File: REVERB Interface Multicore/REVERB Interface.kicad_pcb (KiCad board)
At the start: 2 copper layers, 90.2 x 95.9 mm, 69 parts, among them J1 RPiZeroW, J2 Iridium, J3 APRS, J4 Antenna, J5 UPDI, J6 USBPWR, M1 Stack Mounting Hole, M2 Stack Mounting Hole, M3 Stack Mounting Hole, M4 Stack Mounting Hole, M5 PiMount, M6 PiMount, M7 PiMount, M8 PiMount, U1 IMU, U2 MAX3232, U3 ATtiny1604-SS, U4 TXB0104D, U5 DS3232M

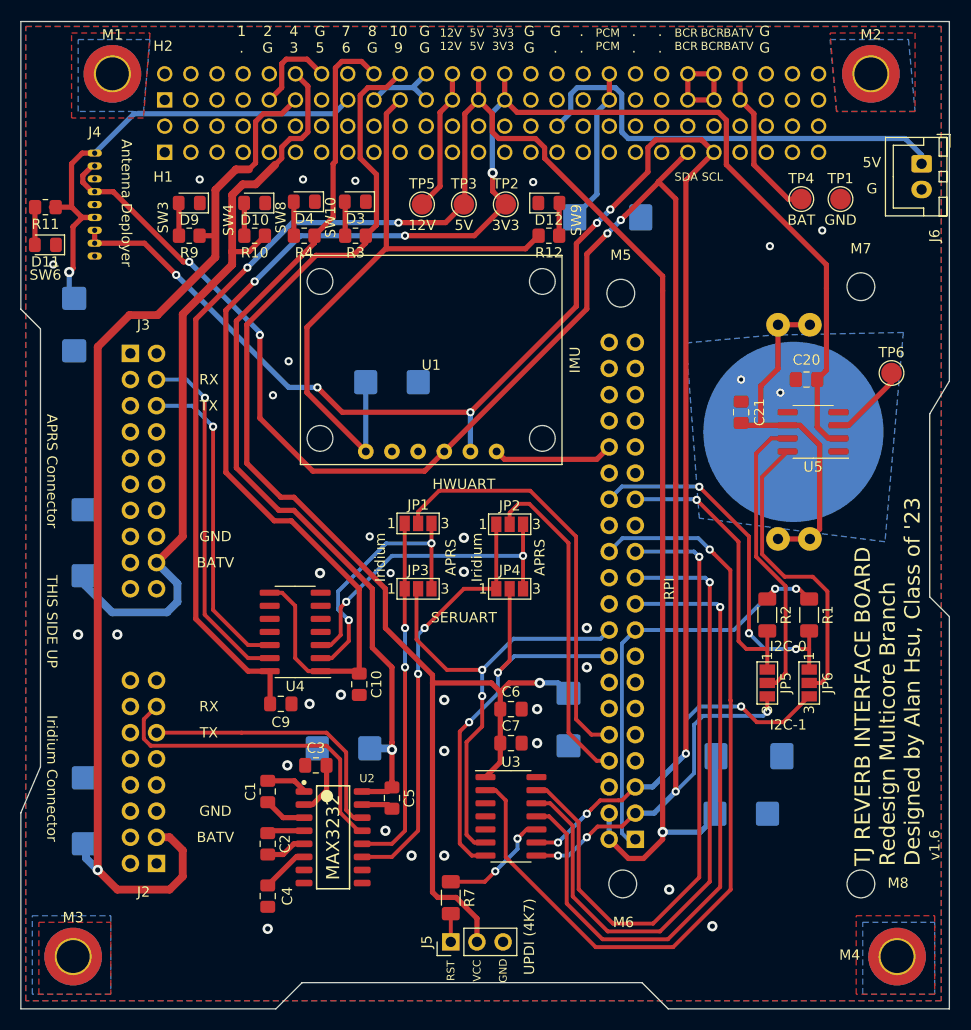
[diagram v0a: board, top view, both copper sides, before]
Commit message: stack conflict checking
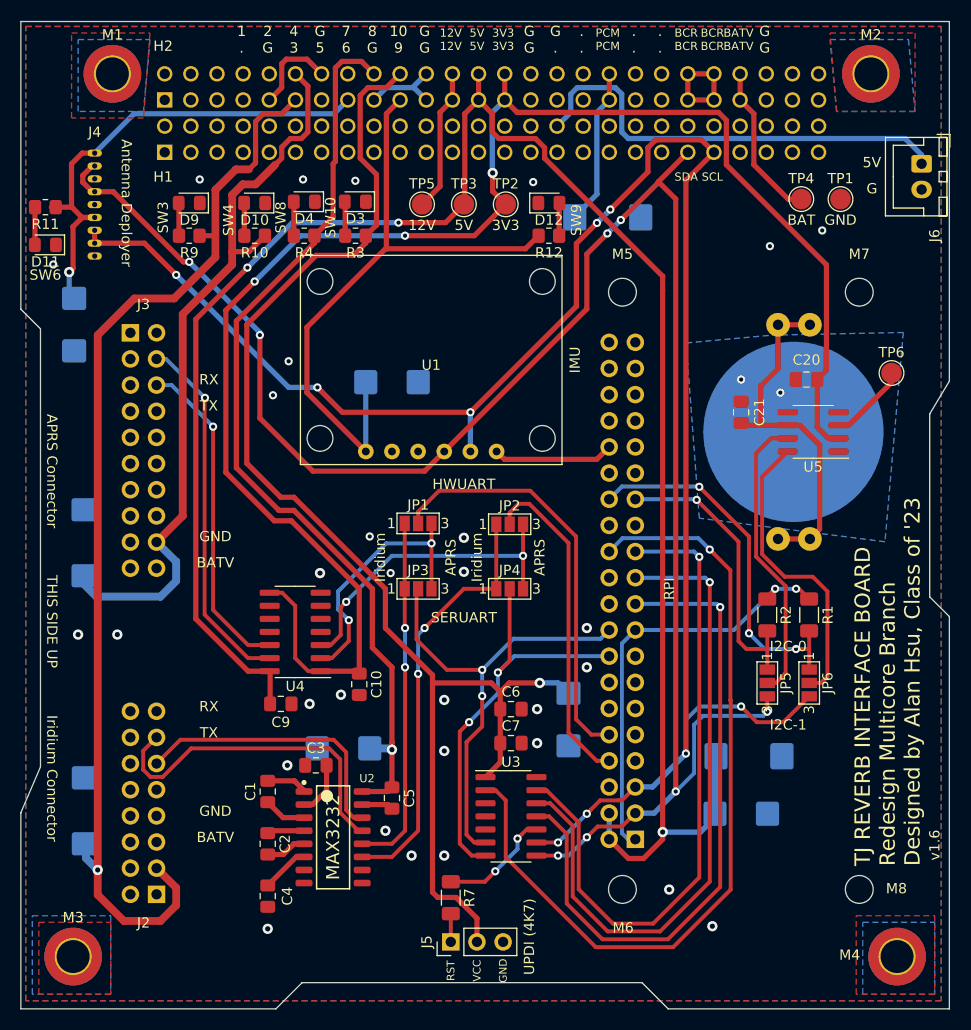
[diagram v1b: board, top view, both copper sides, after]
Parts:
- moved J2 3.00 mm to (120.0, 137.6)
- moved J3 2.00 mm to (117.5, 83.1)
- moved M7 0.56 mm to (188.3, 79.1)
- moved M8 0.56 mm to (188.3, 137.1)
- moved M6 0.54 mm to (165.3, 137.1)
- moved M5 0.19 mm to (165.3, 79.1)
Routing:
- net /SW4: track 75.3 -> 72.7 mm
- net /SW3: track 105.8 -> 107.4 mm
- net /R1IN: track 31.5 -> 32.6 mm
- net /APRSTXSh: track 31.0 -> 31.9 mm
- net /APRSRXSh: track 34.6 -> 35.4 mm
- net /T1OUT: track 26.6 -> 27.3 mm

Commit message: push v2.0
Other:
- board text added: "v2.0"
- board text removed: "v1.6"
